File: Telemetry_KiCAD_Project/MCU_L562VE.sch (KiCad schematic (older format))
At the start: 16 parts

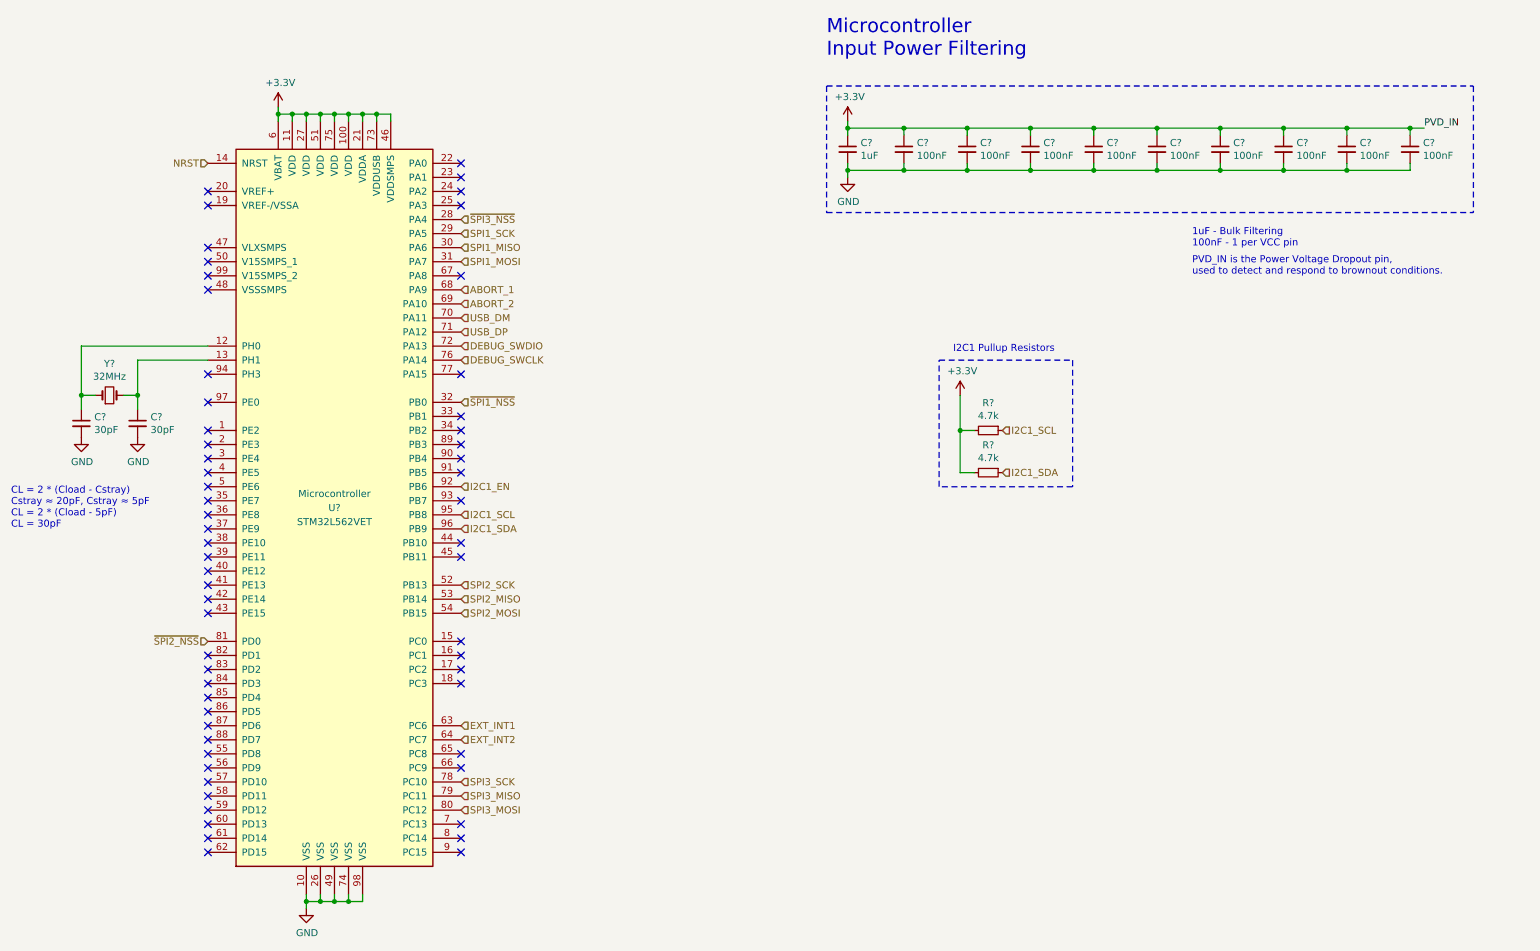
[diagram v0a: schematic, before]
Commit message: Assigned capacitors for new MCU
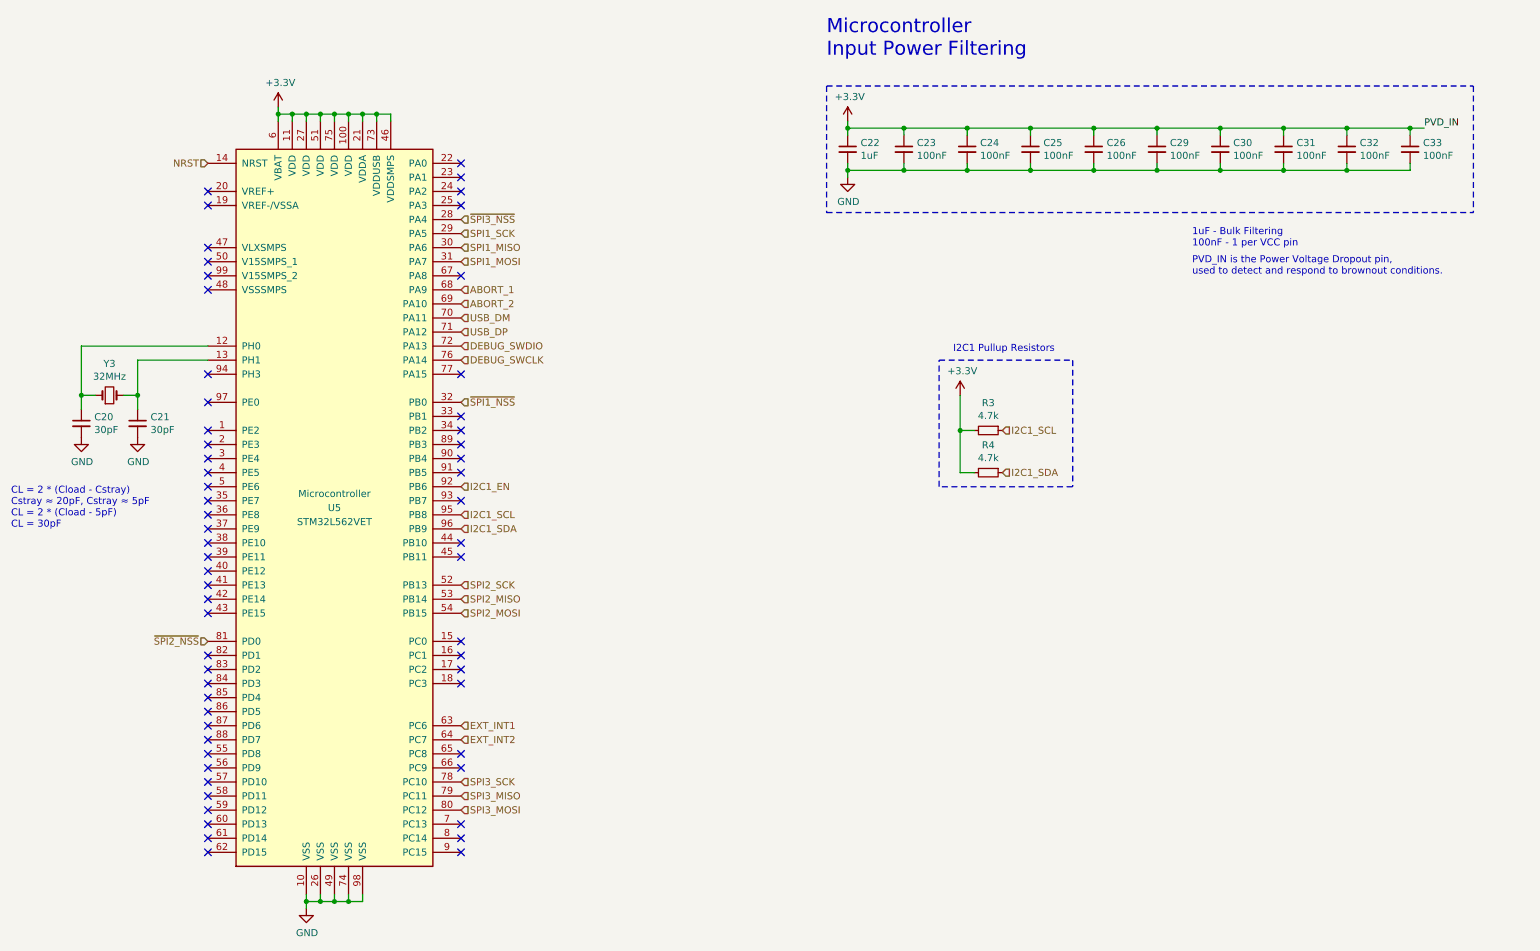
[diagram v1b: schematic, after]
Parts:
- gave numbers to parts that had none: 16
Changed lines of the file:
@@
 EESchema Schematic File Version 4
-LIBS:Telemetry_KiCAD_Project-cache
-EELAYER 29 0
+EELAYER 30 0
 EELAYER END
 $Descr A4 11693 8268
@@
 P 6600 1300
 AR Path="/619FB6DF/61A17DD9" Ref="#PWR?"  Part="1"
-AR Path="/61A107A5/61A17DD9" Ref="#PWR?"  Part="1"
-F 0 "#PWR?" H 6600 1150 50  0001 C CNN
+AR Path="/61A107A5/61A17DD9" Ref="#PWR05"  Part="1"
+F 0 "#PWR05" H 6600 1150 50  0001 C CNN
 F 1 "+3.3V" H 6615 1473 50  0000 C CNN
 F 2 "" H 6600 1300 50  0001 C CNN
@@
 P 6600 1500
 AR Path="/619FB6DF/61A17DDF" Ref="C?"  Part="1"
-AR Path="/61A107A5/61A17DDF" Ref="C?"  Part="1"
-F 0 "C?" H 6692 1546 50  0000 L CNN
+AR Path="/61A107A5/61A17DDF" Ref="C22"  Part="1"
+F 0 "C22" H 6692 1546 50  0000 L CNN
 F 1 "1uF" H 6692 1455 50  0000 L CNN
 F 2 "Capacitor_SMD:C_0603_1608Metric" H 6600 1500 50  0001 C CNN
@@
 P 7000 1500
 AR Path="/619FB6DF/61A17DE5" Ref="C?"  Part="1"
-AR Path="/61A107A5/61A17DE5" Ref="C?"  Part="1"
-F 0 "C?" H 7092 1546 50  0000 L CNN
+AR Path="/61A107A5/61A17DE5" Ref="C23"  Part="1"
+F 0 "C23" H 7092 1546 50  0000 L CNN
 F 1 "100nF" H 7092 1455 50  0000 L CNN
 F 2 "Capacitor_SMD:C_0603_1608Metric" H 7000 1500 50  0001 C CNN
@@
 P 7450 1500
 AR Path="/619FB6DF/61A17DEB" Ref="C?"  Part="1"
-AR Path="/61A107A5/61A17DEB" Ref="C?"  Part="1"
-F 0 "C?" H 7542 1546 50  0000 L CNN
+AR Path="/61A107A5/61A17DEB" Ref="C24"  Part="1"
+F 0 "C24" H 7542 1546 50  0000 L CNN
 F 1 "100nF" H 7542 1455 50  0000 L CNN
 F 2 "Capacitor_SMD:C_0603_1608Metric" H 7450 1500 50  0001 C CNN
@@
 P 8800 1500
 AR Path="/619FB6DF/61A17DF1" Ref="C?"  Part="1"
-AR Path="/61A107A5/61A17DF1" Ref="C?"  Part="1"
-F 0 "C?" H 8892 1546 50  0000 L CNN
+AR Path="/61A107A5/61A17DF1" Ref="C29"  Part="1"
+F 0 "C29" H 8892 1546 50  0000 L CNN
 F 1 "100nF" H 8892 1455 50  0000 L CNN
 F 2 "Capacitor_SMD:C_0603_1608Metric" H 8800 1500 50  0001 C CNN
@@
 P 10600 1500
 AR Path="/619FB6DF/61A17DF7" Ref="C?"  Part="1"
-AR Path="/61A107A5/61A17DF7" Ref="C?"  Part="1"
-F 0 "C?" H 10692 1546 50  0000 L CNN
+AR Path="/61A107A5/61A17DF7" Ref="C33"  Part="1"
+F 0 "C33" H 10692 1546 50  0000 L CNN
 F 1 "100nF" H 10692 1455 50  0000 L CNN
 F 2 "Capacitor_SMD:C_0603_1608Metric" H 10600 1500 50  0001 C CNN
@@
 P 6600 1700
 AR Path="/619FB6DF/61A17DFD" Ref="#PWR?"  Part="1"
-AR Path="/61A107A5/61A17DFD" Ref="#PWR?"  Part="1"
-F 0 "#PWR?" H 6600 1450 50  0001 C CNN
+AR Path="/61A107A5/61A17DFD" Ref="#PWR06"  Part="1"
+F 0 "#PWR06" H 6600 1450 50  0001 C CNN
 F 1 "GND" H 6605 1527 50  0000 C CNN
 F 2 "" H 6600 1700 50  0001 C CNN
@@
 P 7400 3250
 AR Path="/619FB6DF/61A17E24" Ref="#PWR?"  Part="1"
-AR Path="/61A107A5/61A17E24" Ref="#PWR?"  Part="1"
-F 0 "#PWR?" H 7400 3100 50  0001 C CNN
+AR Path="/61A107A5/61A17E24" Ref="#PWR07"  Part="1"
+F 0 "#PWR07" H 7400 3100 50  0001 C CNN
 F 1 "+3.3V" H 7415 3423 50  0000 C CNN
 F 2 "" H 7400 3250 50  0001 C CNN
@@
 P 7600 3500
 AR Path="/619FB6DF/61A17E2A" Ref="R?"  Part="1"
-AR Path="/61A107A5/61A17E2A" Ref="R?"  Part="1"
-F 0 "R?" V 7404 3500 50  0000 C CNN
+AR Path="/61A107A5/61A17E2A" Ref="R3"  Part="1"
+F 0 "R3" V 7404 3500 50  0000 C CNN
 F 1 "4.7k" V 7495 3500 50  0000 C CNN
 F 2 "Resistor_SMD:R_0201_0603Metric" H 7600 3500 50  0001 C CNN
@@
 P 7600 3800
 AR Path="/619FB6DF/61A17E32" Ref="R?"  Part="1"
-AR Path="/61A107A5/61A17E32" Ref="R?"  Part="1"
-F 0 "R?" V 7404 3800 50  0000 C CNN
+AR Path="/61A107A5/61A17E32" Ref="R4"  Part="1"
+F 0 "R4" V 7404 3800 50  0000 C CNN
 F 1 "4.7k" V 7495 3800 50  0000 C CNN
 F 2 "Resistor_SMD:R_0201_0603Metric" H 7600 3800 50  0001 C CNN
@@
 	6450 1050 6450 1950
 $Comp
-L RDT_Custom_Symbols:STM32L562VET U?
+L RDT_Custom_Symbols:STM32L562VET U5
 U 1 1 61A5D08A
 P 2950 1150
-F 0 "U?" H 2950 -1750 50  0000 C CNN
+F 0 "U5" H 2950 -1750 50  0000 C CNN
 F 1 "STM32L562VET" H 2950 -1850 50  0000 C CNN
 F 2 "Package_QFP:LQFP-100_14x14mm_P0.5mm" H 2950 1150 50  0001 C CNN
@@
 $EndComp
 $Comp
-L power:GND #PWR?
+L power:GND #PWR04
 U 1 1 61A6473B
 P 2750 6900
-F 0 "#PWR?" H 2750 6650 50  0001 C CNN
+F 0 "#PWR04" H 2750 6650 50  0001 C CNN
 F 1 "GND" H 2755 6727 50  0000 C CNN
 F 2 "" H 2750 6900 50  0001 C CNN
@@
 Connection ~ 2750 6850
 $Comp
-L power:+3.3V #PWR?
+L power:+3.3V #PWR03
 U 1 1 61A6DB50
 P 2550 1200
-F 0 "#PWR?" H 2550 1050 50  0001 C CNN
+F 0 "#PWR03" H 2550 1050 50  0001 C CNN
 F 1 "+3.3V" H 2565 1373 50  0000 C CNN
 F 2 "" H 2550 1200 50  0001 C CNN
@@
 P 7900 1500
 AR Path="/619FB6DF/61A89EEB" Ref="C?"  Part="1"
-AR Path="/61A107A5/61A89EEB" Ref="C?"  Part="1"
-F 0 "C?" H 7992 1546 50  0000 L CNN
+AR Path="/61A107A5/61A89EEB" Ref="C25"  Part="1"
+F 0 "C25" H 7992 1546 50  0000 L CNN
 F 1 "100nF" H 7992 1455 50  0000 L CNN
 F 2 "Capacitor_SMD:C_0603_1608Metric" H 7900 1500 50  0001 C CNN
@@
 P 8350 1500
 AR Path="/619FB6DF/61A89EF1" Ref="C?"  Part="1"
-AR Path="/61A107A5/61A89EF1" Ref="C?"  Part="1"
-F 0 "C?" H 8442 1546 50  0000 L CNN
+AR Path="/61A107A5/61A89EF1" Ref="C26"  Part="1"
+F 0 "C26" H 8442 1546 50  0000 L CNN
 F 1 "100nF" H 8442 1455 50  0000 L CNN
 F 2 "Capacitor_SMD:C_0603_1608Metric" H 8350 1500 50  0001 C CNN
@@
 P 9250 1500
 AR Path="/619FB6DF/61AA18EF" Ref="C?"  Part="1"
-AR Path="/61A107A5/61AA18EF" Ref="C?"  Part="1"
-F 0 "C?" H 9342 1546 50  0000 L CNN
+AR Path="/61A107A5/61AA18EF" Ref="C30"  Part="1"
+F 0 "C30" H 9342 1546 50  0000 L CNN
 F 1 "100nF" H 9342 1455 50  0000 L CNN
 F 2 "Capacitor_SMD:C_0603_1608Metric" H 9250 1500 50  0001 C CNN
@@
 P 9700 1500
 AR Path="/619FB6DF/61AA2382" Ref="C?"  Part="1"
-AR Path="/61A107A5/61AA2382" Ref="C?"  Part="1"
-F 0 "C?" H 9792 1546 50  0000 L CNN
+AR Path="/61A107A5/61AA2382" Ref="C31"  Part="1"
+F 0 "C31" H 9792 1546 50  0000 L CNN
 F 1 "100nF" H 9792 1455 50  0000 L CNN
 F 2 "Capacitor_SMD:C_0603_1608Metric" H 9700 1500 50  0001 C CNN
@@
 P 10150 1500
 AR Path="/619FB6DF/61AA2953" Ref="C?"  Part="1"
-AR Path="/61A107A5/61AA2953" Ref="C?"  Part="1"
-F 0 "C?" H 10242 1546 50  0000 L CNN
+AR Path="/61A107A5/61AA2953" Ref="C32"  Part="1"
+F 0 "C32" H 10242 1546 50  0000 L CNN
 F 1 "100nF" H 10242 1455 50  0000 L CNN
 F 2 "Capacitor_SMD:C_0603_1608Metric" H 10150 1500 50  0001 C CNN
@@
 P 1150 3450
 AR Path="/619FB6DF/61ADFE6A" Ref="C?"  Part="1"
-AR Path="/61A107A5/61ADFE6A" Ref="C?"  Part="1"
-F 0 "C?" H 1242 3496 50  0000 L CNN
+AR Path="/61A107A5/61ADFE6A" Ref="C20"  Part="1"
+F 0 "C20" H 1242 3496 50  0000 L CNN
 F 1 "30pF" H 1242 3405 50  0000 L CNN
 F 2 "Capacitor_SMD:C_0603_1608Metric" H 1150 3450 50  0001 C CNN
@@
 P 1550 3550
 AR Path="/619FB6DF/61ADFE70" Ref="#PWR?"  Part="1"
-AR Path="/61A107A5/61ADFE70" Ref="#PWR?"  Part="1"
-F 0 "#PWR?" H 1550 3300 50  0001 C CNN
+AR Path="/61A107A5/61ADFE70" Ref="#PWR02"  Part="1"
+F 0 "#PWR02" H 1550 3300 50  0001 C CNN
 F 1 "GND" H 1555 3377 50  0000 C CNN
 F 2 "" H 1550 3550 50  0001 C CNN
@@
 P 1150 3550
 AR Path="/619FB6DF/61ADFE76" Ref="#PWR?"  Part="1"
-AR Path="/61A107A5/61ADFE76" Ref="#PWR?"  Part="1"
-F 0 "#PWR?" H 1150 3300 50  0001 C CNN
+AR Path="/61A107A5/61ADFE76" Ref="#PWR01"  Part="1"
+F 0 "#PWR01" H 1150 3300 50  0001 C CNN
 F 1 "GND" H 1155 3377 50  0000 C CNN
 F 2 "" H 1150 3550 50  0001 C CNN
@@
 P 1550 3450
 AR Path="/619FB6DF/61ADFE7C" Ref="C?"  Part="1"
-AR Path="/61A107A5/61ADFE7C" Ref="C?"  Part="1"
-F 0 "C?" H 1642 3496 50  0000 L CNN
+AR Path="/61A107A5/61ADFE7C" Ref="C21"  Part="1"
+F 0 "C21" H 1642 3496 50  0000 L CNN
 F 1 "30pF" H 1642 3405 50  0000 L CNN
 F 2 "Capacitor_SMD:C_0603_1608Metric" H 1550 3450 50  0001 C CNN
@@
 P 1350 3250
 AR Path="/619FB6DF/61ADFE82" Ref="Y?"  Part="1"
-AR Path="/61A107A5/61ADFE82" Ref="Y?"  Part="1"
-F 0 "Y?" H 1350 3475 50  0000 C CNN
+AR Path="/61A107A5/61ADFE82" Ref="Y3"  Part="1"
+F 0 "Y3" H 1350 3475 50  0000 C CNN
 F 1 "32MHz" H 1350 3384 50  0000 C CNN
 F 2 "Crystal:Crystal_SMD_0603-2Pin_6.0x3.5mm" H 1350 3250 50  0001 C CNN

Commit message: Added RSD Duplexer Footprint, rearranged RF matching networks
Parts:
- R3, R4: footprint Resistor_SMD:R_0201_0603Metric -> Resistors:0603
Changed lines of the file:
@@
 F 0 "R3" V 7404 3500 50  0000 C CNN
 F 1 "4.7k" V 7495 3500 50  0000 C CNN
-F 2 "Resistor_SMD:R_0201_0603Metric" H 7600 3500 50  0001 C CNN
+F 2 "Resistors:0603" H 7600 3500 50  0001 C CNN
 F 3 "~" H 7600 3500 50  0001 C CNN
 	1    7600 3500
@@
 F 0 "R4" V 7404 3800 50  0000 C CNN
 F 1 "4.7k" V 7495 3800 50  0000 C CNN
-F 2 "Resistor_SMD:R_0201_0603Metric" H 7600 3800 50  0001 C CNN
+F 2 "Resistors:0603" H 7600 3800 50  0001 C CNN
 F 3 "~" H 7600 3800 50  0001 C CNN
 	1    7600 3800
